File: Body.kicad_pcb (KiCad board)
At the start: 2 copper layers, 101.5 x 21.5 mm, 20 parts, among them J10 6pin_conn, J11 1pin_conn, J12 1pin_conn, J13 1pin_conn, J14 1pin_conn, J7 6pin_conn, J8 6pin_conn, J9 6pin_conn

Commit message: Footprint was Jacked for LED - it's been fixed
foot print for led was incorrect.  It aslo seems that some pad resistors are needed
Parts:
- added R3: 33 ohm, Resistors_SMD:R_Array_Concave_2x0603, B.Cu at (87.0, 94.7)
- added R4: 33 ohm, Resistors_SMD:R_Array_Concave_2x0603, B.Cu at (117.0, 94.2)
- added R5: 33 ohm, Resistors_SMD:R_Array_Concave_2x0603, B.Cu at (165.4, 87.7)
- D1, D2, D3, D4: footprint MyLib:APA102-2020 -> MyLib:APA102-2020_style_2
- R1, R2: value R_Small_US -> 33 ohm; footprint Resistors_SMD:R_0805 -> Resistors_SMD:R_Array_Concave_2x0603; moved to F.Cu
- moved R2 78.2 mm to (87.0, 92.3), turned to 180 degrees
- moved R1 37.3 mm to (129.6, 95.8), turned to 180 degrees
- moved C1 3.01 mm to (126.2, 93.3), turned to 0 degrees
- moved C2 2.71 mm to (72.5, 93.5), turned to 270 degrees
- moved C3 2.71 mm to (72.5, 93.5), turned to 270 degrees
- moved D2 2.30 mm to (75.0, 93.5), turned to 90 degrees
- moved D3 2.30 mm to (75.0, 93.5), turned to 270 degrees
- turned C4 to 0 degrees
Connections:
- D2 pad 4: Net-(D1-Pad3) -> Net-(D2-Pad4)
- D2 pad 5: Net-(D1-Pad2) -> Net-(D2-Pad5)
- D3 pad 4: Net-(D2-Pad3) -> Net-(D3-Pad4)
- D3 pad 5: Net-(D2-Pad2) -> Net-(D3-Pad5)
- D4 pad 4: Net-(D3-Pad3) -> Net-(D4-Pad4)
- D4 pad 5: Net-(D3-Pad2) -> Net-(D4-Pad5)
- J13 pad 1: Net-(D1-Pad5) -> Net-(J13-Pad1)
- J14 pad 1: Net-(D1-Pad4) -> Net-(J14-Pad1)
- R1 pad 1: Net-(J10-Pad6) -> Net-(J14-Pad1)
- R1 pad 2: GND -> Net-(J13-Pad1)
- R2 pad 1: Net-(J10-Pad5) -> Net-(D1-Pad3)
- R2 pad 2: GND -> Net-(D1-Pad2)
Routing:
- net +5V: track 16.5 -> 132.7 mm, vias 4 -> 7
- net Net-(D1-Pad4): track 27.1 -> 1.77 mm, vias 2 -> 0
- net Net-(J14-Pad1): track 0.00 -> 24.0 mm
- net GND: track 27.7 -> 6.68 mm, vias 11 -> 24
- net Net-(D1-Pad5): track 22.3 -> 1.77 mm, vias 1 -> 0
- net Net-(J13-Pad1): track 0.00 -> 20.3 mm, vias 0 -> 2
- net Net-(D1-Pad3): track 53.3 -> 39.0 mm
- net Net-(D1-Pad2): track 52.5 -> 39.0 mm
- net Net-(D2-Pad2): track 3.05 -> 16.0 mm
- net Net-(D3-Pad5): track 0.00 -> 12.1 mm
- net Net-(D2-Pad5): track 0.00 -> 12.1 mm
- net Net-(D2-Pad4): track 0.00 -> 11.9 mm
- net Net-(D3-Pad3): track 52.9 -> 41.1 mm
- net Net-(D2-Pad3): track 2.88 -> 14.0 mm
- net Net-(D3-Pad4): track 0.00 -> 10.3 mm
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- added copper zone on F.Cu, net GND
- removed copper zone on F.Cu, net +5V
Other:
- board size 101.5 x 21.5 mm -> 101.5 x 19.8 mm
- rule solder_mask_min_width: 0.25 -> 0.254

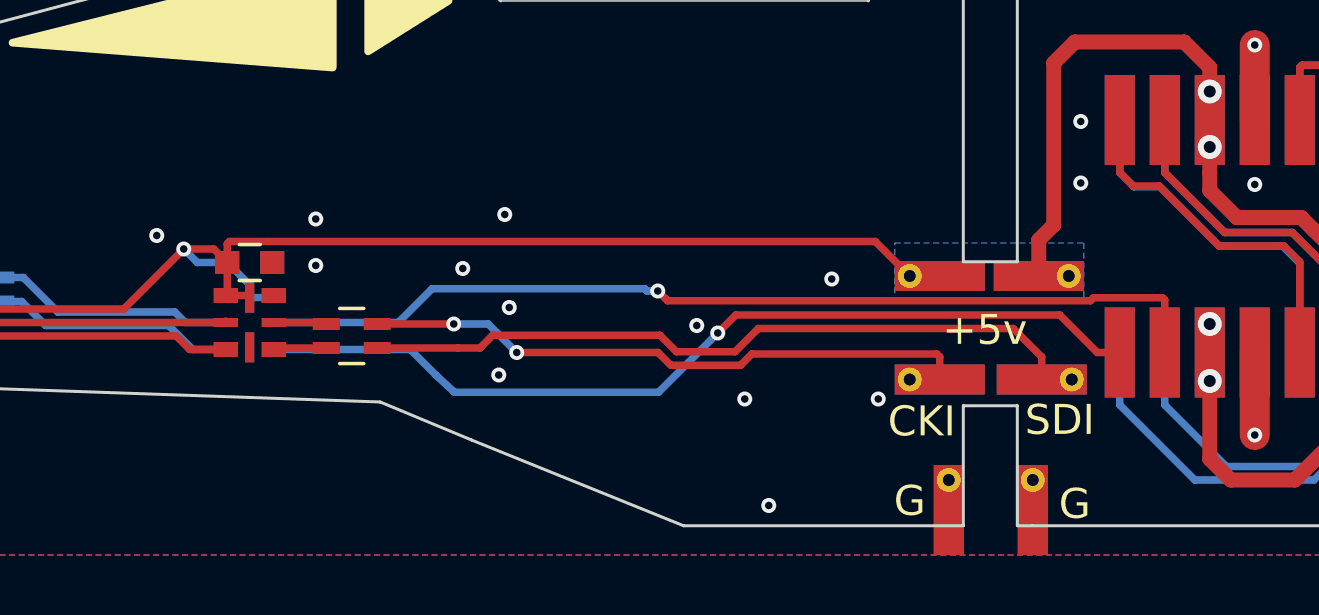
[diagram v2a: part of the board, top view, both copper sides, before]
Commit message: Board Fixes fort bad footprint
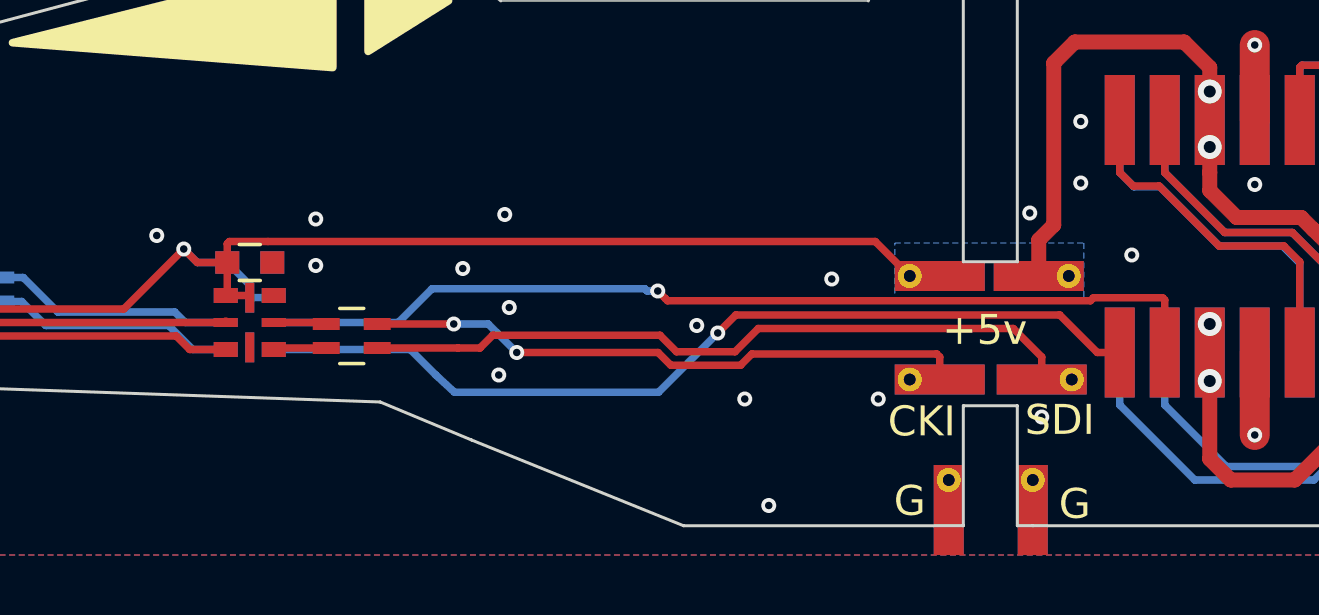
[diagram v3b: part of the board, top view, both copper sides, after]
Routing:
- net GND: vias 24 -> 27
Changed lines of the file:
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@@
   (general
     (thickness 1.6)
-    (drawings 54)
-    (tracks 292)
+    (drawings 56)
+    (tracks 295)
     (zones 0)
     (modules 23)
@@
     )
   )
+  (gr_poly (pts (xy 153 85.2) (xy 148.8 85.2) (xy 148.8 83.6) (xy 153 83.6)) (layer B.Mask) (width 0.1))
+  (gr_poly (pts (xy 153 85.2) (xy 148.8 85.2) (xy 148.8 83.6) (xy 153 83.6)) (layer F.Mask) (width 0.1))
   (dimension 19.78 (width 0.15) (layer Dwgs.User)
     (gr_text "19.780 mm" (at 173.95 92.24 90) (layer Dwgs.User)
@@
   (segment (start 125.45 93.35) (end 124.45 93.35) (width 0.25) (layer B.Cu) (net 1))
   (segment (start 124.45 93.35) (end 124 92.9) (width 0.25) (layer B.Cu) (net 1))
-  (segment (start 125 92.9) (end 125.45 93.35) (width 0.25) (layer F.Cu) (net 1))
-  (segment (start 124 92.9) (end 125 92.9) (width 0.25) (layer F.Cu) (net 1))
   (segment (start 158.2 87.65) (end 158.2 86.85) (width 0.5) (layer F.Cu) (net 1))
   (via (at 158.2 87.65) (size 0.8) (drill 0.4) (layers F.Cu B.Cu) (net 1))
@@
   (segment (start 77.45 91.4) (end 77.89998 91.84998) (width 0.25) (layer F.Cu) (net 1))
   (segment (start 77.89998 91.84998) (end 84.54998 91.84998) (width 0.25) (layer F.Cu) (net 1))
+  (segment (start 124.45 93.35) (end 124 92.9) (width 0.25) (layer F.Cu) (net 1))
+  (segment (start 125.45 93.35) (end 124.45 93.35) (width 0.25) (layer F.Cu) (net 1))
   (segment (start 159.7 96.35) (end 159.7 99.1) (width 1) (layer F.Cu) (net 2))
   (via (at 159.7 99.1) (size 0.5) (drill 0.25) (layers F.Cu B.Cu) (net 2))
@@
   (via (at 147.15 97.9) (size 0.5) (drill 0.25) (layers F.Cu B.Cu) (net 2))
   (via (at 142.7 97.9) (size 0.5) (drill 0.25) (layers F.Cu B.Cu) (net 2))
+  (via (at 152.2 91.7) (size 0.5) (drill 0.25) (layers F.Cu B.Cu) (net 2))
+  (via (at 155.6 93.1) (size 0.5) (drill 0.25) (layers F.Cu B.Cu) (net 2))
+  (via (at 152.6 98.5) (size 0.5) (drill 0.25) (layers F.Cu B.Cu) (net 2))
   (segment (start 91.481805 95.031805) (end 107.114289 95.031805) (width 0.25) (layer F.Cu) (net 3))
   (segment (start 107.61359 95.5) (end 107.9136 95.80001) (width 0.25) (layer F.Cu) (net 3))
